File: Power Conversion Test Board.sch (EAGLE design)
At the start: 46 parts, among them U1 LM2678, U2 LM2678

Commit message: ripped board up and started over
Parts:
- removed C13: .01uF, Seeed-Capacitor:TANTALUM-SMD-10UF-16V-10%(AVX-A)
- removed C5: 470nF, SparkFun-Capacitors:470NF-0402-16V-10%
- removed C8, C9: 150uf, Seeed-Capacitor:TANTALUM-SMD-10UF-16V-10%(AVX-A)
- added C14, C29, C30, C31: 10uF, PowerComponents:C-TANTALUM(10UF_150UF)
- added J5, J6: (no value), SparkFun-Connectors:BANANA_CONN
- C1, C15, C16, C17, C18: device SparkFun-Capacitors:10UF-1206-6.3V-20% -> PowerComponents:C-TANTALUM(10UF_150UF)
- C10, C24: value 100uF -> 150uF; device Seeed-Capacitor:TANTALUM-SMD-10UF-16V-10%(AVX-A) -> PowerComponents:C-TANTALUM(10UF_150UF)
- C11, C25: value 10uF -> 150uF; device Seeed-Capacitor:TANTALUM-SMD-10UF-16V-10%(AVX-A) -> PowerComponents:C-TANTALUM(10UF_150UF)
- C12, C26: value .1uF -> 150uF; device Seeed-Capacitor:TANTALUM-SMD-10UF-16V-10%(AVX-A) -> PowerComponents:C-TANTALUM(10UF_150UF)
- C19: value 470nF -> 100uF; device SparkFun-Capacitors:470NF-0402-16V-10% -> PowerComponents:C-TANTALUM(10UF_150UF)
- C2: value 10uF -> .1uF; device SparkFun-Capacitors:10UF-1206-6.3V-20% -> PowerComponents:C-TANTALUM(10UF_150UF)
- C21: value 150uf -> 10uF; device Seeed-Capacitor:TANTALUM-SMD-10UF-16V-10%(AVX-A) -> PowerComponents:C-TANTALUM(10UF_150UF)
- C22: value 150uf -> .1uF; device Seeed-Capacitor:TANTALUM-SMD-10UF-16V-10%(AVX-A) -> PowerComponents:C-TANTALUM(10UF_150UF)
- C23: value 150uf -> .01uF; device Seeed-Capacitor:TANTALUM-SMD-10UF-16V-10%(AVX-A) -> PowerComponents:C-TANTALUM(10UF_150UF)
- C27: value .01uF -> 100uF; device Seeed-Capacitor:TANTALUM-SMD-10UF-16V-10%(AVX-A) -> PowerComponents:C-TANTALUM(10UF_150UF)
- C3: value 10uF -> 0.47uF; device SparkFun-Capacitors:10UF-1206-6.3V-20% -> rcl:C-EUC0603
- C4: value 10uF -> .01uF; device SparkFun-Capacitors:10UF-1206-6.3V-20% -> PowerComponents:C-TANTALUM(10UF_150UF)
- C7: value 150uf -> 0.47uF; device Seeed-Capacitor:TANTALUM-SMD-10UF-16V-10%(AVX-A) -> rcl:C-EUC0603
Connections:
- net +12V: now also C14.+, C15.+, C16.+, C17.+, C18.+, C29.+, C3.1, C30.+, C31.+, C7.1; no longer C1.2, C15.2, C16.2, C17.2, C18.2, C19.2, C2.2, C3.2, C4.2, C5.2
- net +3.3V: now also J5.1
- net +5V: now also C10.+, C11.+, C12.+, J6.1; no longer C7.+, C8.+, C9.+
- net +5V_3.3V: now also C24.+, C25.+, C26.+; no longer C21.+, C22.+, C23.+
- net 12VGND: now also C1.+, C14.-, C15.-, C16.-, C17.-, C18.-, C19.+, C2.+, C21.+, C22.+, C23.+, C29.-, C3.2, C30.-, C31.-, C4.+, C7.2; no longer C1.1, C10.+, C11.+, C12.+, C13.+, C15.1, C16.1, C17.1, C18.1, C19.1, C2.1, C24.+, C25.+, C26.+, C3.1, C4.1, C5.1
- net 3.3VGND: now also C1.-, C19.-, C2.-, C4.-, R3.2, R5.1, U$10.1, U$3.P$1, U$3.P$3, U2.GND, U2.TABGND
- net 5VGND: now also C21.-, C22.-, C23.-; no longer C10.-, C11.-, C12.-, C13.-, C24.-, C25.-, C26.-, R3.2, R5.1, U$10.1, U$3.P$1, U$3.P$3, U2.GND, U2.TABGND
- net N$4: now also C24.-, C25.-, C26.-; no longer C21.-, C22.-, C23.-
- net N$8: now also C10.-, C11.-, C12.-; no longer C7.-, C8.-, C9.-
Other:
- moved on the sheet: C3

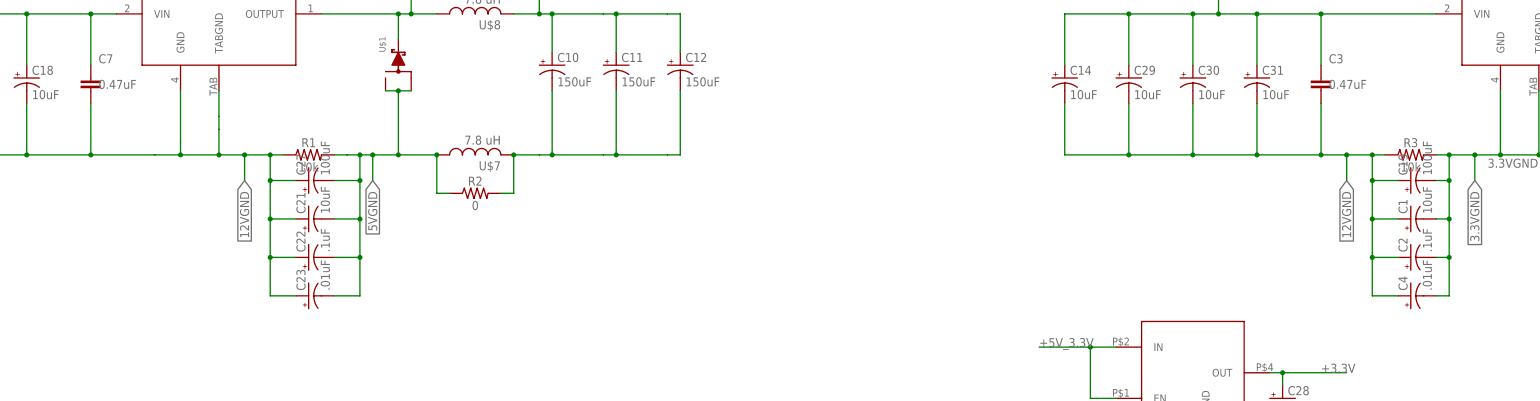
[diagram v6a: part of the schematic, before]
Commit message: Replaced components and routed some more.
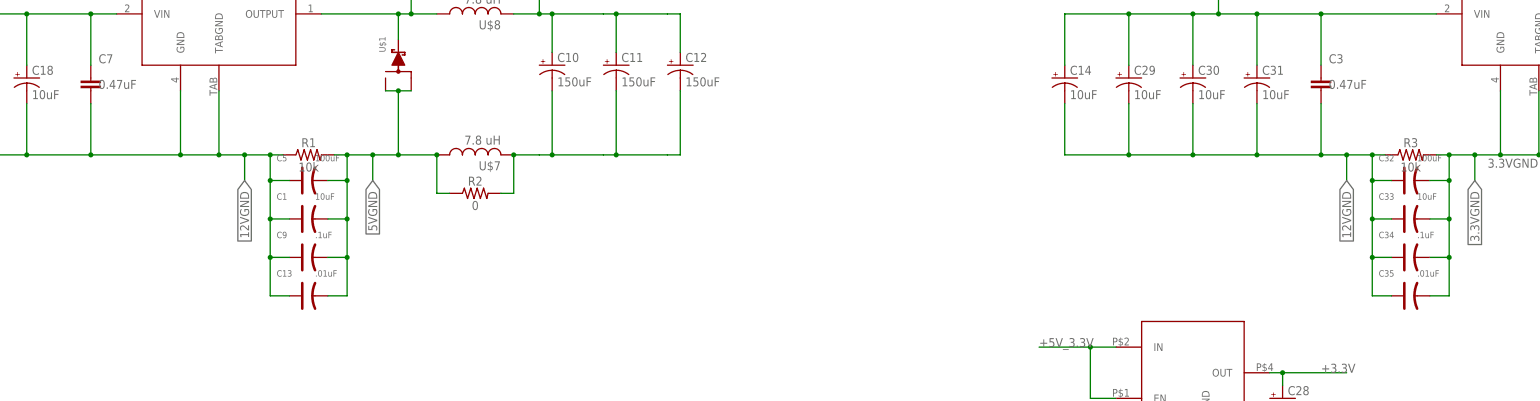
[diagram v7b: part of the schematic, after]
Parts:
- removed C19, C27: 100uF, PowerComponents:C-TANTALUM(10UF_150UF)
- removed C2, C22: .1uF, PowerComponents:C-TANTALUM(10UF_150UF)
- removed C21: 10uF, PowerComponents:C-TANTALUM(10UF_150UF)
- removed C23, C4: .01uF, PowerComponents:C-TANTALUM(10UF_150UF)
- added C13, C35: .01uF, Seeed-Capacitor:TANTALUM-SMD-10UF-16V-10%(AVX-A)
- added C32, C5: 100uF, Seeed-Capacitor:TANTALUM-SMD-10UF-16V-10%(AVX-A)
- added C33: 10uF, Seeed-Capacitor:TANTALUM-SMD-10UF-16V-10%(AVX-A)
- added C34, C9: .1uF, Seeed-Capacitor:TANTALUM-SMD-10UF-16V-10%(AVX-A)
- C1: device PowerComponents:C-TANTALUM(10UF_150UF) -> Seeed-Capacitor:TANTALUM-SMD-10UF-16V-10%(AVX-A)
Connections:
- net 12VGND: now also C13.+, C32.+, C33.+, C34.+, C35.+, C5.+, C9.+; no longer C19.+, C2.+, C21.+, C22.+, C23.+, C27.+, C4.+
- net 3.3VGND: now also C32.-, C33.-, C34.-, C35.-; no longer C1.-, C19.-, C2.-, C4.-
- net 5VGND: now also C1.-, C13.-, C5.-, C9.-; no longer C21.-, C22.-, C23.-, C27.-

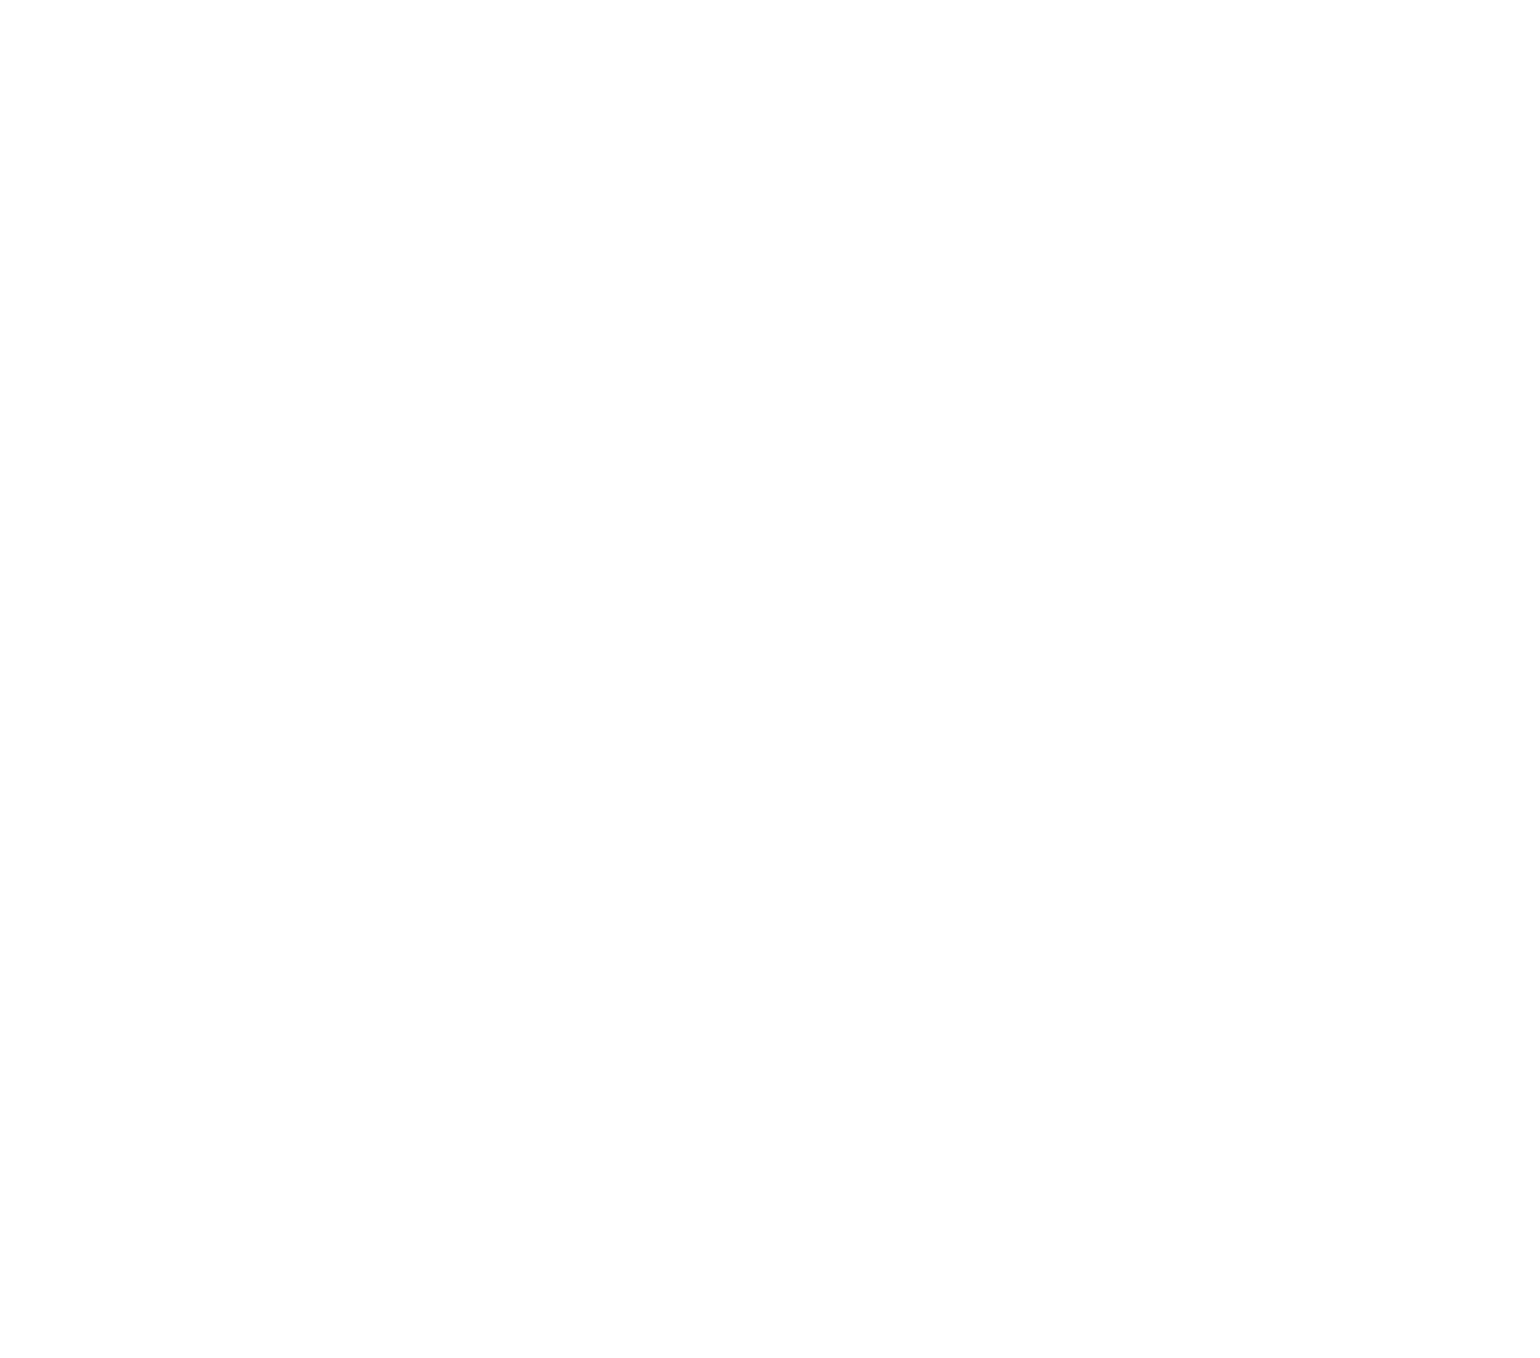
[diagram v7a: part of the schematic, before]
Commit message: Added connectors
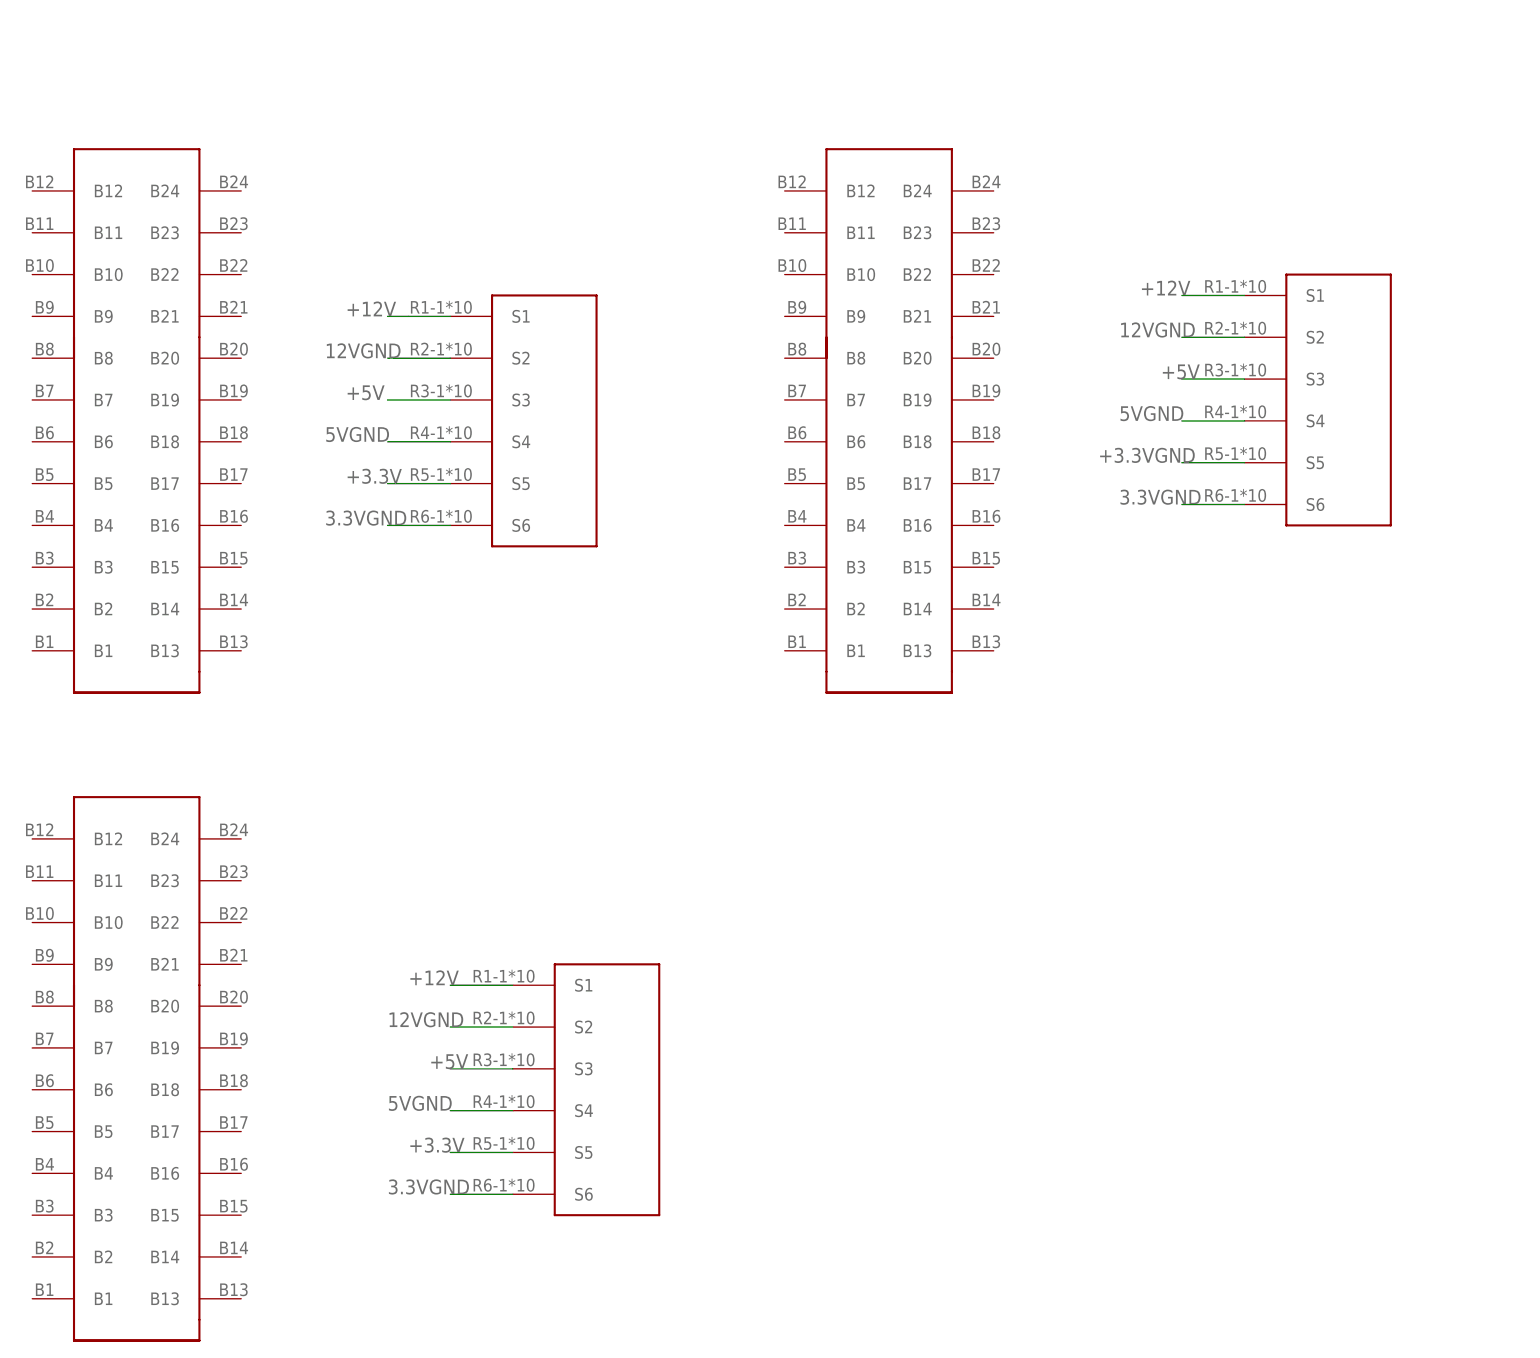
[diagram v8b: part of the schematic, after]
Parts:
- added U$11, U$2, U$6: ET60T_2, ET60T:ET60T_2
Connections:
- new net +3.3VGND: U$6G$2.S5
- net +12V: now also U$11G$2.S1, U$2G$2.S1, U$6G$2.S1
- net +3.3V: now also U$11G$2.S5, U$2G$2.S5
- net +5V: now also U$11G$2.S3, U$2G$2.S3, U$6G$2.S3
- net 12VGND: now also U$11G$2.S2, U$2G$2.S2, U$6G$2.S2
- net 3.3VGND: now also U$11G$2.S6, U$2G$2.S6, U$6G$2.S6
- net 5VGND: now also U$11G$2.S4, U$2G$2.S4, U$6G$2.S4
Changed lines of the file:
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@@
 <part name="C35" library="Seeed-Capacitor" library_urn="urn:adsk.eagle:library:464" deviceset="TANTALUM-SMD-10UF-16V-10%(AVX-A)" device="" package3d_urn="urn:adsk.eagle:package:32380/1" value=".01uF"/>
 <part name="C1" library="Seeed-Capacitor" library_urn="urn:adsk.eagle:library:464" deviceset="TANTALUM-SMD-10UF-16V-10%(AVX-A)" device="" package3d_urn="urn:adsk.eagle:package:32380/1" value="10uF"/>
+<part name="FRAME3" library="frames" library_urn="urn:adsk.eagle:library:229" deviceset="A4L-LOC" device=""/>
+<part name="U$2" library="ET60T" deviceset="ET60T_2" device=""/>
+<part name="U$6" library="ET60T" deviceset="ET60T_2" device=""/>
+<part name="U$11" library="ET60T" deviceset="ET60T_2" device=""/>
 </parts>
 <sheets>
@@
 <instance part="C35" gate="G$1" x="388.62" y="86.36"/>
 <instance part="C1" gate="G$1" x="170.18" y="101.6"/>
+<instance part="FRAME3" gate="G$1" x="0" y="-180.34">
+<attribute name="DRAWING_NAME" x="217.17" y="-165.1" size="2.54" layer="94"/>
+<attribute name="LAST_DATE_TIME" x="217.17" y="-170.18" size="2.286" layer="94"/>
+<attribute name="SHEET" x="230.505" y="-175.26" size="2.54" layer="94"/>
+</instance>
+<instance part="U$2" gate="G$1" x="40.64" y="-55.88"/>
+<instance part="U$2" gate="G$2" x="91.44" y="-53.34"/>
+<instance part="U$6" gate="G$1" x="132.08" y="-55.88"/>
+<instance part="U$6" gate="G$2" x="187.96" y="-50.8"/>
+<instance part="U$11" gate="G$1" x="40.64" y="-134.62"/>
+<instance part="U$11" gate="G$2" x="99.06" y="-134.62"/>
 </instances>
 <busses>
@@
 <wire x1="73.66" y1="104.14" x2="68.58" y2="104.14" width="0.1524" layer="91"/>
 </segment>
+<segment>
+<pinref part="U$2" gate="G$2" pin="S1"/>
+<wire x1="78.74" y1="-40.64" x2="73.66" y2="-40.64" width="0.1524" layer="91"/>
+<wire x1="73.66" y1="-40.64" x2="71.12" y2="-40.64" width="0.1524" layer="91"/>
+<label x="66.04" y="-40.64" size="1.778" layer="95"/>
+</segment>
+<segment>
+<pinref part="U$6" gate="G$2" pin="S1"/>
+<wire x1="175.26" y1="-38.1" x2="167.64" y2="-38.1" width="0.1524" layer="91"/>
+<label x="162.56" y="-38.1" size="1.778" layer="95"/>
+</segment>
+<segment>
+<pinref part="U$11" gate="G$2" pin="S1"/>
+<wire x1="86.36" y1="-121.92" x2="78.74" y2="-121.92" width="0.1524" layer="91"/>
+<label x="73.66" y="-121.92" size="1.778" layer="95"/>
+</segment>
 </net>
 <net name="+5V" class="0">
@@
 <label x="66.04" y="81.28" size="1.778" layer="95" rot="R180" xref="yes"/>
 </segment>
+<segment>
+<pinref part="U$2" gate="G$2" pin="S3"/>
+<wire x1="78.74" y1="-50.8" x2="71.12" y2="-50.8" width="0.1524" layer="91"/>
+<label x="66.04" y="-50.8" size="1.778" layer="95"/>
+</segment>
+<segment>
+<pinref part="U$6" gate="G$2" pin="S3"/>
+<wire x1="175.26" y1="-48.26" x2="167.64" y2="-48.26" width="0.1524" layer="91"/>
+<label x="165.1" y="-48.26" size="1.778" layer="95"/>
+</segment>
+<segment>
+<pinref part="U$11" gate="G$2" pin="S3"/>
+<wire x1="86.36" y1="-132.08" x2="78.74" y2="-132.08" width="0.1524" layer="91"/>
+<label x="76.2" y="-132.08" size="1.778" layer="95"/>
+</segment>
 </net>
 <net name="N$1" class="0">
@@
 <wire x1="441.96" y1="66.04" x2="434.34" y2="66.04" width="0.1524" layer="91"/>
 <label x="434.34" y="66.04" size="1.778" layer="95" rot="R180" xref="yes"/>
+</segment>
+<segment>
+<pinref part="U$2" gate="G$2" pin="S5"/>
+<wire x1="78.74" y1="-60.96" x2="71.12" y2="-60.96" width="0.1524" layer="91"/>
+<label x="66.04" y="-60.96" size="1.778" layer="95"/>
+</segment>
+<segment>
+<pinref part="U$11" gate="G$2" pin="S5"/>
+<wire x1="86.36" y1="-142.24" x2="78.74" y2="-142.24" width="0.1524" layer="91"/>
+<label x="73.66" y="-142.24" size="1.778" layer="95"/>
 </segment>
 </net>
@@
 <wire x1="396.24" y1="86.36" x2="396.24" y2="93.98" width="0.1524" layer="91"/>
 <junction x="396.24" y="93.98"/>
+</segment>
+<segment>
+<pinref part="U$2" gate="G$2" pin="S6"/>
+<wire x1="78.74" y1="-66.04" x2="71.12" y2="-66.04" width="0.1524" layer="91"/>
+<label x="63.5" y="-66.04" size="1.778" layer="95"/>
+</segment>
+<segment>
+<pinref part="U$6" gate="G$2" pin="S6"/>
+<wire x1="175.26" y1="-63.5" x2="167.64" y2="-63.5" width="0.1524" layer="91"/>
+<label x="160.02" y="-63.5" size="1.778" layer="95"/>
+</segment>
+<segment>
+<pinref part="U$11" gate="G$2" pin="S6"/>
+<wire x1="86.36" y1="-147.32" x2="78.74" y2="-147.32" width="0.1524" layer="91"/>
+<label x="71.12" y="-147.32" size="1.778" layer="95"/>
 </segment>
 </net>
@@
 <junction x="162.56" y="101.6"/>
 </segment>
+<segment>
+<pinref part="U$2" gate="G$2" pin="S2"/>
+<wire x1="78.74" y1="-45.72" x2="71.12" y2="-45.72" width="0.1524" layer="91"/>
+<label x="63.5" y="-45.72" size="1.778" layer="95"/>
+</segment>
+<segment>
+<pinref part="U$6" gate="G$2" pin="S2"/>
+<wire x1="175.26" y1="-43.18" x2="167.64" y2="-43.18" width="0.1524" layer="91"/>
+<label x="160.02" y="-43.18" size="1.778" layer="95"/>
+</segment>
+<segment>
+<pinref part="U$11" gate="G$2" pin="S2"/>
+<wire x1="86.36" y1="-127" x2="78.74" y2="-127" width="0.1524" layer="91"/>
+<label x="71.12" y="-127" size="1.778" layer="95"/>
+</segment>
 </net>
 <net name="5VGND" class="0">
@@
 <label x="66.04" y="88.9" size="1.778" layer="95" rot="R180" xref="yes"/>
 </segment>
-</net>
+<segment>
+<pinref part="U$2" gate="G$2" pin="S4"/>
+<wire x1="78.74" y1="-55.88" x2="71.12" y2="-55.88" width="0.1524" layer="91"/>
+<label x="63.5" y="-55.88" size="1.778" layer="95"/>
+</segment>
+<segment>
+<pinref part="U$6" gate="G$2" pin="S4"/>
+<wire x1="175.26" y1="-53.34" x2="167.64" y2="-53.34" width="0.1524" layer="91"/>
+<label x="160.02" y="-53.34" size="1.778" layer="95"/>
+</segment>
+<segment>
+<pinref part="U$11" gate="G$2" pin="S4"/>
+<wire x1="86.36" y1="-137.16" x2="78.74" y2="-137.16" width="0.1524" layer="91"/>
+<label x="71.12" y="-137.16" size="1.778" layer="95"/>
+</segment>
+</net>
+<net name="+3.3VGND" class="0">
+<segment>
+<pinref part="U$6" gate="G$2" pin="S5"/>
+<wire x1="175.26" y1="-58.42" x2="167.64" y2="-58.42" width="0.1524" layer="91"/>
+<label x="157.48" y="-58.42" size="1.778" layer="95"/>
+</segment>
+</net>
